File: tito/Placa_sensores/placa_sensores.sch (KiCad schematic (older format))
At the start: 9 parts, among them P1 CONN_3X2

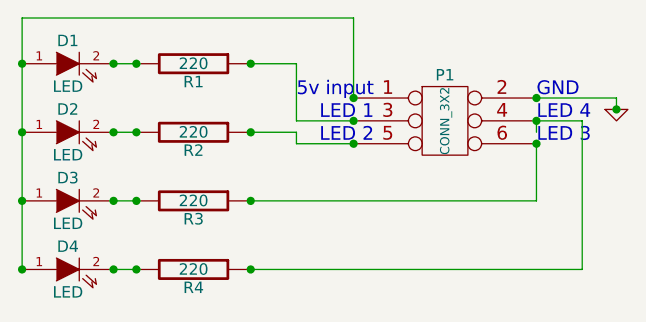
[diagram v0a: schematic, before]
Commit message: subi .lib y .mod cny70 + algo te placa sensores
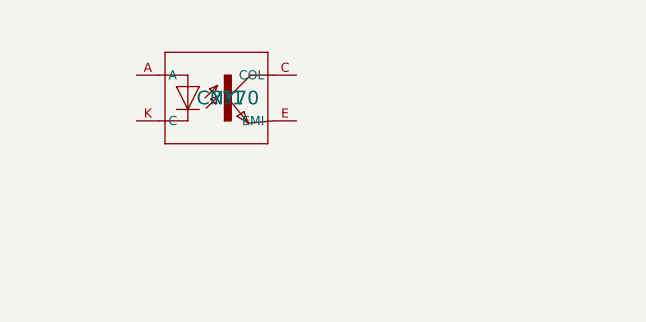
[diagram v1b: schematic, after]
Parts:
- removed D1, D2, D3, D4: LED, symbol LED
- removed P1: CONN_3X2, symbol CONN_3X2
- removed R1, R2, R3, R4: 220, symbol R
- added ??1: CNY70, symbol CNY70
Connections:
- net labels removed: GND
- wire segments 21 -> 0
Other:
- note removed: "5v input"
- note removed: "GND"
- note removed: "LED 1\n"
- note removed: "LED 2"
- note removed: "LED 3"
- note removed: "LED 4"
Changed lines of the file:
@@
-EESchema Schematic File Version 2  date Tue 12 Apr 2011 03:40:38 PM ART
+EESchema Schematic File Version 2  date Fri 09 Sep 2011 09:48:26 PM ART
+LIBS:cny70
 LIBS:power
 LIBS:device
@@
 LIBS:contrib
 LIBS:valves
-LIBS:reg_5v
 LIBS:placa_sensores-cache
 EELAYER 24  0
@@
 Sheet 1 1
 Title ""
-Date "12 apr 2011"
+Date "10 sep 2011"
 Rev ""
 Comp ""
@@
 Comment4 ""
 $EndDescr
-Wire Wire Line
-	7000 4200 7000 4450
-Wire Wire Line
-	7200 4750 7200 4100
-Wire Wire Line
-	7200 4750 5750 4750
-Connection ~ 7350 4050
-Wire Wire Line
-	5750 4150 5950 4150
-Wire Wire Line
-	4750 3650 6200 3650
-Wire Wire Line
-	7000 4000 7350 4000
-Wire Wire Line
-	7000 4150 7000 4100
-Connection ~ 7000 4000
-Connection ~ 7000 4100
-Connection ~ 7000 4200
-Connection ~ 6200 4200
-Connection ~ 6200 4100
-Connection ~ 6200 4000
-Connection ~ 5750 4750
-Connection ~ 5750 4450
-Connection ~ 5750 4150
-Connection ~ 5750 3850
-Connection ~ 5150 3850
-Connection ~ 5250 3850
-Connection ~ 5250 4150
-Connection ~ 5150 4150
-Connection ~ 5150 4450
-Connection ~ 5250 4450
-Wire Wire Line
-	5150 4450 5250 4450
-Wire Wire Line
-	5150 4750 5250 4750
-Wire Wire Line
-	5150 3850 5250 3850
-Connection ~ 4750 4150
-Connection ~ 4750 3850
-Connection ~ 4750 4450
-Wire Wire Line
-	5150 4150 5250 4150
-Connection ~ 4750 4750
-Connection ~ 5250 4750
-Connection ~ 5150 4750
-Wire Wire Line
-	5750 3850 5950 3850
-Wire Wire Line
-	5950 3850 5950 4100
-Wire Wire Line
-	5950 4100 6200 4100
-Wire Wire Line
-	7350 4000 7350 4050
-Wire Wire Line
-	4750 3650 4750 4750
-Wire Wire Line
-	6200 3650 6200 4000
-Wire Wire Line
-	7000 4100 7200 4100
-Wire Wire Line
-	7000 4450 5750 4450
-Wire Wire Line
-	5950 4150 5950 4200
-Wire Wire Line
-	5950 4200 6200 4200
 $Comp
-L GND #PWR01
-U 1 1 4DA3121B
-P 7350 4050
-F 0 "#PWR01" H 7350 4050 30  0001 C CNN
-F 1 "GND" H 7350 3980 30  0001 C CNN
-	1    7350 4050
+L CNY70 ??1
+U 1 1 4E6AB34B
+P 5650 4000
+F 0 "??1" H 5650 4000 60  0000 C CNN
+F 1 "CNY70" H 5650 4000 60  0000 C CNN
+	1    5650 4000
 	1    0    0    -1
 $EndComp
-Text Notes 6050 4200 0    60   ~ 0
-LED 2
-Text Notes 6050 4100 0    60   ~ 0
-LED 1\n
-Text Notes 7000 4200 0    60   ~ 0
-LED 3
-Text Notes 7000 4100 0    60   ~ 0
-LED 4
-Text Notes 7000 4000 0    60   ~ 0
-GND
-Text Notes 5950 4000 0    60   ~ 0
-5v input
-$Comp
-L LED D3
-U 1 1 4DA308A8
-P 4950 4450
-F 0 "D3" H 4950 4550 50  0000 C CNN
-F 1 "LED" H 4950 4350 50  0000 C CNN
-	1    4950 4450
-	1    0    0    -1
-$EndComp
-$Comp
-L R R3
-U 1 1 4DA308A7
-P 5500 4450
-F 0 "R3" V 5580 4450 50  0000 C CNN
-F 1 "220" V 5500 4450 50  0000 C CNN
-	1    5500 4450
-	0    1    1    0
-$EndComp
-$Comp
-L CONN_3X2 P1
-U 1 1 4DA30867
-P 6600 4150
-F 0 "P1" H 6600 4400 50  0000 C CNN
-F 1 "CONN_3X2" V 6600 4200 40  0000 C CNN
-	1    6600 4150
-	1    0    0    -1
-$EndComp
-$Comp
-L R R4
-U 1 1 4DA30433
-P 5500 4750
-F 0 "R4" V 5580 4750 50  0000 C CNN
-F 1 "220" V 5500 4750 50  0000 C CNN
-	1    5500 4750
-	0    1    1    0
-$EndComp
-$Comp
-L R R2
-U 1 1 4DA301BB
-P 5500 4150
-F 0 "R2" V 5580 4150 50  0000 C CNN
-F 1 "220" V 5500 4150 50  0000 C CNN
-	1    5500 4150
-	0    1    1    0
-$EndComp
-$Comp
-L R R1
-U 1 1 4DA301B3
-P 5500 3850
-F 0 "R1" V 5580 3850 50  0000 C CNN
-F 1 "220" V 5500 3850 50  0000 C CNN
-	1    5500 3850
-	0    1    1    0
-$EndComp
-$Comp
-L LED D4
-U 1 1 4DA30122
-P 4950 4750
-F 0 "D4" H 4950 4850 50  0000 C CNN
-F 1 "LED" H 4950 4650 50  0000 C CNN
-	1    4950 4750
-	1    0    0    -1
-$EndComp
-$Comp
-L LED D2
-U 1 1 4DA30121
-P 4950 4150
-F 0 "D2" H 4950 4250 50  0000 C CNN
-F 1 "LED" H 4950 4050 50  0000 C CNN
-	1    4950 4150
-	1    0    0    -1
-$EndComp
-$Comp
-L LED D1
-U 1 1 4DA30119
-P 4950 3850
-F 0 "D1" H 4950 3950 50  0000 C CNN
-F 1 "LED" H 4950 3750 50  0000 C CNN
-	1    4950 3850
-	1    0    0    -1
-$EndComp
